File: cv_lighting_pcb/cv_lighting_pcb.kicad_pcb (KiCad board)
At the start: 2 copper layers, 27 parts, among them Q1 2N3906, U1 Current Driver, U2 Camera Input, U3 VO617A, U4 Barrel Jack

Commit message: added some notes to schematic
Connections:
- net Net-(U1-Vin+) renamed +30V
- R3 pad 1: Net-(U2-3) -> Net-(U2-PWM_Input)
- U2 pad 1: /PWM input -> Net-(U2-PWM_Input)
- U2 pad 2: GND -> Net-(U2-PWM_GND)
- U3 pad 2: Net-(U2-4) -> Net-(U2-PWM_GND)
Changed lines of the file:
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@@
   (net 11 "Net-(Q1-B)")
   (net 12 "Net-(Q1-C)")
-  (net 13 "/PWM input")
+  (net 13 "+30V")
   (net 14 "Net-(R3-Pad2)")
-  (net 15 "Net-(U1-Vin+)")
+  (net 15 "Net-(U2-PWM_Input)")
   (net 16 "GND")
-  (net 17 "Net-(U2-3)")
-  (net 18 "Net-(U2-4)")
-  (net 19 "unconnected-(U4-PadA2)")
-  (net 20 "unconnected-(U4-PadC)")
+  (net 17 "Net-(U2-PWM_GND)")
+  (net 18 "unconnected-(U4-PadA2)")
+  (net 19 "unconnected-(U4-PadC)")
   (footprint "cv_lighting_footprints:D3V3M1U2S9-7" (layer "F.Cu")
     (at 179.8828 130.7084)
@@
       (stroke (width 0.1) (type solid)) (layer "F.Fab"))
     (pad "1" smd roundrect (at -1.0375 0) (size 1.175 1.45) (layers "F.Cu" "F.Paste" "F.Mask") (roundrect_rratio 0.212766)
-      (net 15 "Net-(U1-Vin+)") (pintype "passive"))
+      (net 13 "+30V") (pintype "passive"))
     (pad "2" smd roundrect (at 1.0375 0) (size 1.175 1.45) (layers "F.Cu" "F.Paste" "F.Mask") (roundrect_rratio 0.212766)
       (net 16 "GND") (pintype "passive"))
@@
       (net 14 "Net-(R3-Pad2)") (pintype "passive"))
     (pad "2" smd rect (at -3.72 6.604) (size 2 1.78) (layers "F.Cu" "F.Paste" "F.Mask")
-      (net 18 "Net-(U2-4)") (pintype "passive"))
+      (net 17 "Net-(U2-PWM_GND)") (pintype "passive"))
     (pad "3" smd rect (at 3.9 6.604) (size 2 1.78) (layers "F.Cu" "F.Paste" "F.Mask")
       (net 9 "Net-(D15-A)") (pintype "passive"))
@@
       (net 10 "Net-(Q1-E)") (pinfunction "REF") (pintype "input") (solder_mask_margin 0.102))
     (pad "5" smd rect (at 6.6525 17.272 90) (size 1.02 1.905) (layers "F.Cu" "F.Paste" "F.Mask")
-      (net 15 "Net-(U1-Vin+)") (pinfunction "Vin+") (pintype "input") (solder_mask_margin 0.102))
+      (net 13 "+30V") (pinfunction "Vin+") (pintype "input") (solder_mask_margin 0.102))
     (pad "6" smd rect (at 9.9845 19.685 90) (size 1.02 1.905) (layers "F.Cu" "F.Paste" "F.Mask")
       (solder_mask_margin 0.102))
@@
       (stroke (width 0.1) (type solid)) (layer "F.Fab"))
     (pad "1" smd roundrect (at -1 0) (size 1.2 1.4) (layers "F.Cu" "F.Paste" "F.Mask") (roundrect_rratio 0.208333)
-      (net 17 "Net-(U2-3)") (pintype "passive"))
+      (net 15 "Net-(U2-PWM_Input)") (pintype "passive"))
     (pad "2" smd roundrect (at 1 0) (size 1.2 1.4) (layers "F.Cu" "F.Paste" "F.Mask") (roundrect_rratio 0.208333)
       (net 14 "Net-(R3-Pad2)") (pintype "passive"))
@@
     (pad "" np_thru_hole circle (at 0 2.25) (size 1.6 1.6) (drill 1.6) (layers "*.Cu" "*.Mask"))
     (pad "A1" smd rect (at -5.5 2.25) (size 2 2) (layers "F.Cu" "F.Paste" "F.Mask")
-      (net 15 "Net-(U1-Vin+)") (pintype "passive") (solder_mask_margin 0.102))
+      (net 13 "+30V") (pintype "passive") (solder_mask_margin 0.102))
     (pad "A2" smd rect (at -5.5 -3.95) (size 2 2) (layers "F.Cu" "F.Paste" "F.Mask")
-      (net 19 "unconnected-(U4-PadA2)") (pintype "passive") (solder_mask_margin 0.102))
+      (net 18 "unconnected-(U4-PadA2)") (pintype "passive") (solder_mask_margin 0.102))
     (pad "B" smd rect (at 5.5 2.25) (size 2 2) (layers "F.Cu" "F.Paste" "F.Mask")
       (net 16 "GND") (pintype "passive") (solder_mask_margin 0.102))
     (pad "C" smd rect (at 5.5 -3.95) (size 2 2) (layers "F.Cu" "F.Paste" "F.Mask")
-      (net 20 "unconnected-(U4-PadC)") (pintype "passive") (solder_mask_margin 0.102))
+      (net 19 "unconnected-(U4-PadC)") (pintype "passive") (solder_mask_margin 0.102))
   )
   (footprint "Connector_PinSocket_2.54mm:PinSocket_1x02_P2.54mm_Vertical_SMD_Pin1Left" (layer "F.Cu")
@@
       (stroke (width 0.1) (type solid)) (layer "F.Fab"))
     (pad "1" smd rect (at -1.65 -1.27) (size 1.9 1) (layers "F.Cu" "F.Paste" "F.Mask")
-      (net 13 "/PWM input") (pinfunction "Camera_input") (pintype "input"))
+      (net 15 "Net-(U2-PWM_Input)") (pinfunction "PWM_Input") (pintype "passive"))
     (pad "2" smd rect (at 1.65 1.27) (size 1.9 1) (layers "F.Cu" "F.Paste" "F.Mask")
-      (net 16 "GND") (pinfunction "GND") (pintype "input"))
+      (net 17 "Net-(U2-PWM_GND)") (pinfunction "PWM_GND") (pintype "passive"))
     (model "${KICAD6_3DMODEL_DIR}/Connector_PinSocket_2.54mm.3dshapes/PinSocket_1x02_P2.54mm_Vertical_SMD_Pin1Left.wrl"
       (offset (xyz 0 0 0))

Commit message: updates to lighting pcb
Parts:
- moved U2 39.9 mm to (121.0, 144.5)
- moved D11 32.0 mm to (242.4, 104.7)
- moved U1 31.2 mm to (118.7, 53.2)
- moved D4 30.9 mm to (237.5, 125.1)
- moved D3 28.0 mm to (238.8, 87.0)
- moved D12 26.4 mm to (227.8, 135.2)
- moved D5 26.0 mm to (212.7, 149.9)
- moved D10 24.1 mm to (227.2, 64.7)
- moved D2 23.5 mm to (213.4, 58.6)
- moved D13 21.9 mm to (190.7, 149.8)
- moved D9 21.1 mm to (195.4, 50.7)
- moved D14 18.4 mm to (161.5, 139.0)
- moved D6 18.1 mm to (174.0, 149.9)
- moved D7 13.8 mm to (148.0, 127.6)
- moved C2 13.7 mm to (131.4, 103.8)
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
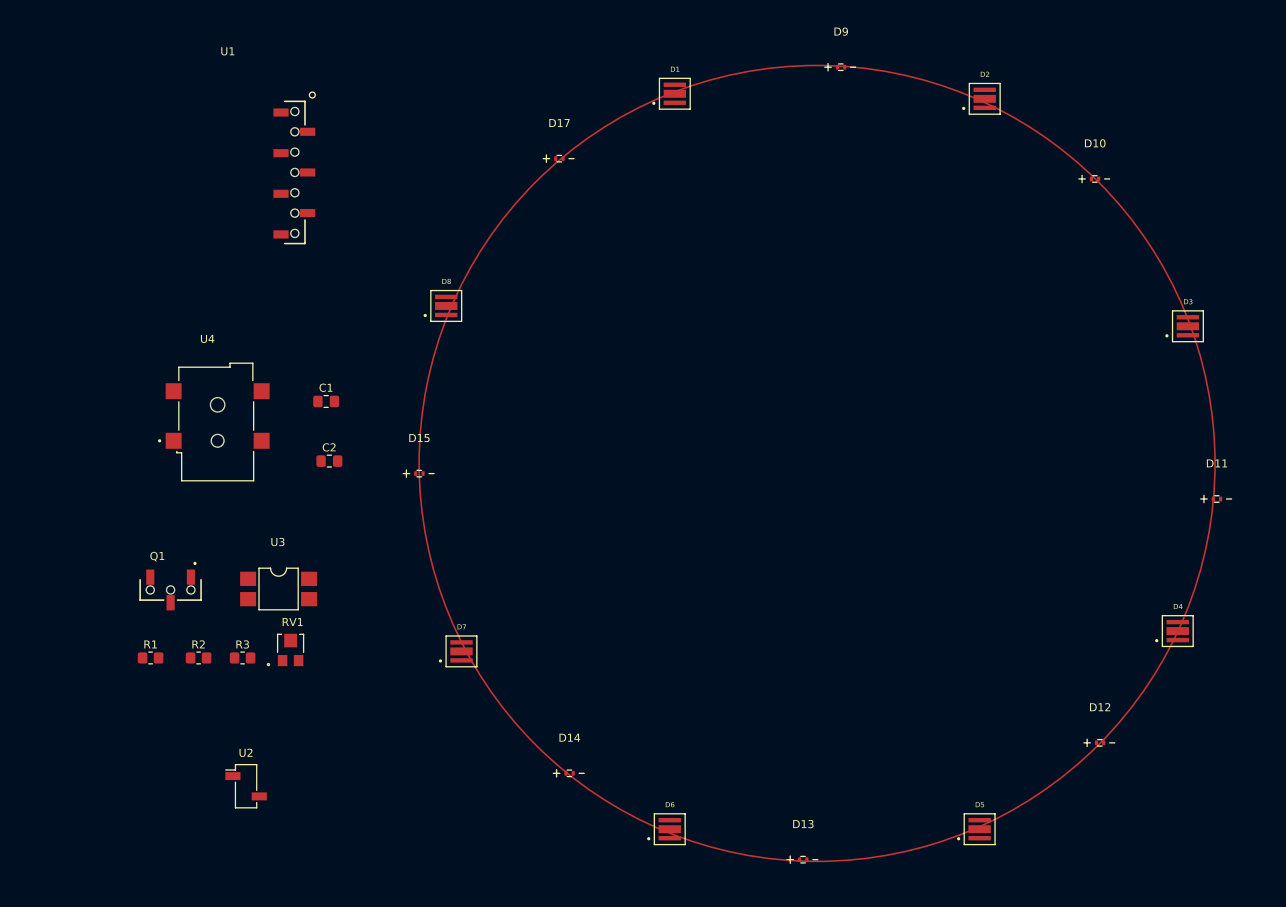
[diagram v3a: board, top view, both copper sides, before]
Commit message: initial routing and edge cuts for pcb
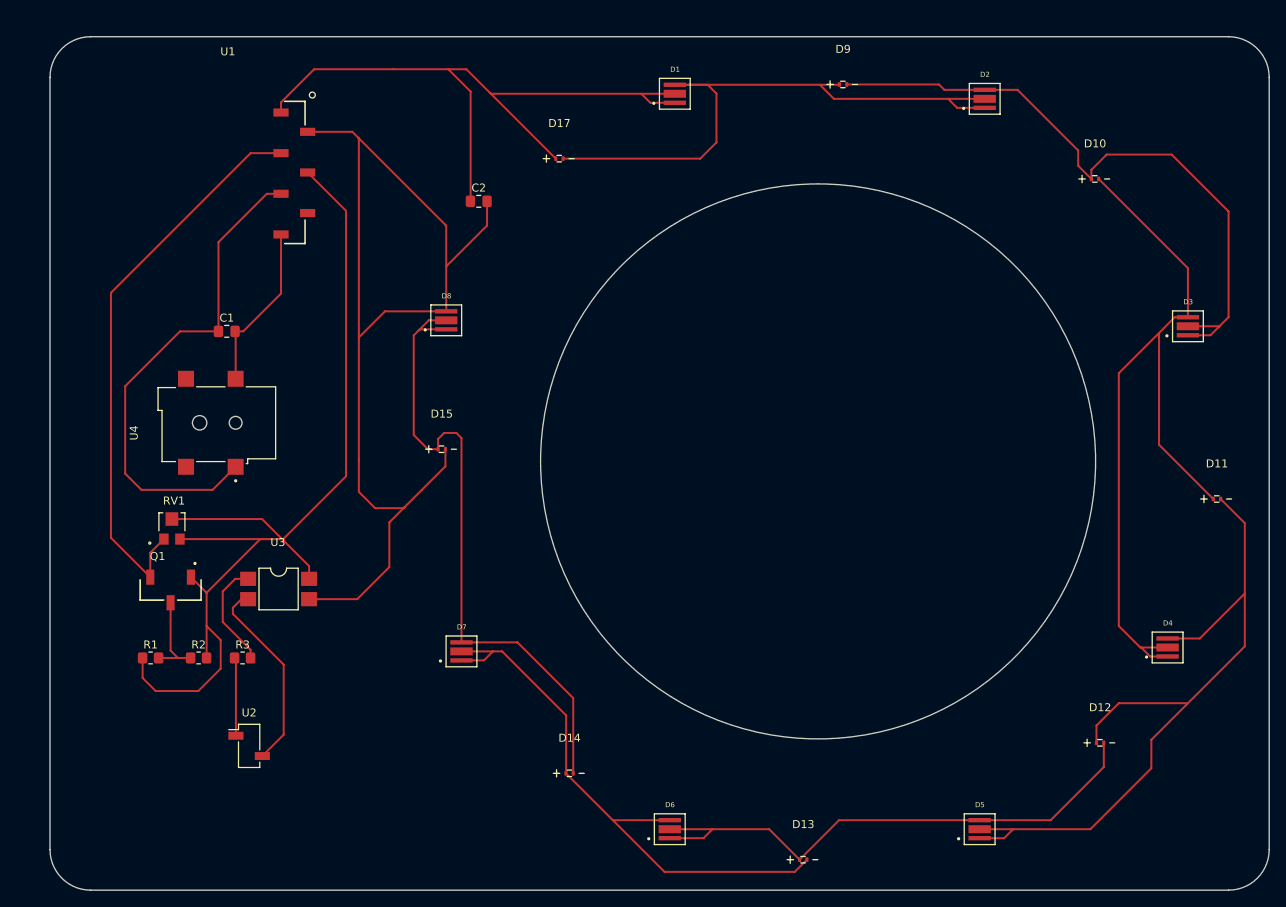
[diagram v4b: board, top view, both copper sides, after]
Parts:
- moved C2 37.5 mm to (150.1, 71.4)
- moved RV1 21.2 mm to (111.8, 112.3)
- moved C1 15.2 mm to (118.6, 87.6)
- moved U2 5.06 mm to (121.4, 139.4)
- moved D15 4.13 mm to (145.5, 98.5)
- moved D4 2.41 mm to (236.2, 127.1)
- moved D9 2.17 mm to (195.7, 52.9)
- moved D8 1.80 mm to (146.1, 86.3)
- turned U4 to 90 degrees
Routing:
- net Net-(D15-A): track 0.00 -> 135.6 mm
- net Net-(Q1-E): track 0.00 -> 128.4 mm
- net Net-(D10-A): track 0.00 -> 99.6 mm
- net Net-(D11-A): track 0.00 -> 95.8 mm
- net Net-(D1-A): track 0.00 -> 87.5 mm
- net Net-(D10-K): track 0.00 -> 81.8 mm
- net Net-(D14-A): track 0.00 -> 81.1 mm
- net Net-(D1-K): track 0.00 -> 78.7 mm
- net Net-(Q1-C): track 0.00 -> 71.5 mm
- net Net-(D13-A): track 0.00 -> 71.0 mm
- net Net-(D12-A): track 0.00 -> 69.5 mm
- net +30V: track 0.00 -> 62.7 mm
- net Net-(U2-PWM_GND): track 0.00 -> 24.6 mm
- net GND: track 0.00 -> 21.0 mm
- net Net-(R3-Pad2): track 0.00 -> 13.6 mm
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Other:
- board outline added: 152.4 x 106.7 mm
- board text added: "Double check radius of circle based on camera"
- board text added: "checker says every is connected but still double check also parts may change"

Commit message: updates to lighting pcb, now smaller
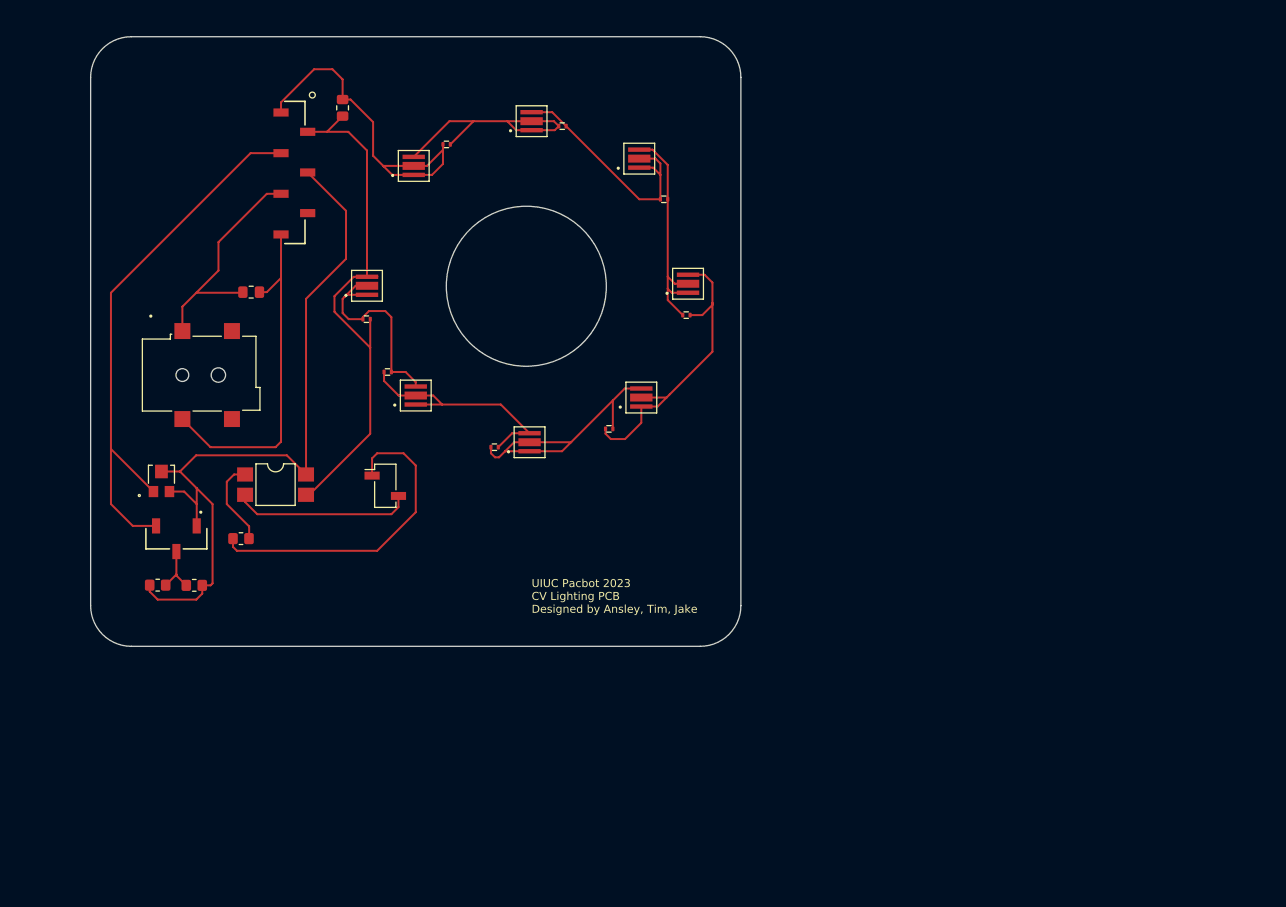
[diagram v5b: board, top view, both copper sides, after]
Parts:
- moved D4 75.2 mm to (176.3, 81.7)
- moved D12 72.8 mm to (166.4, 95.9)
- moved D3 71.7 mm to (170.2, 66.0)
- moved D11 70.2 mm to (176.1, 81.7)
- moved D5 68.6 mm to (170.4, 95.9)
- moved D13 64.4 mm to (152.1, 98.2)
- moved D2 56.7 mm to (156.7, 61.4)
- moved D14 55.1 mm to (138.7, 88.8)
- moved D10 53.9 mm to (173.3, 67.2)
- moved D6 51.4 mm to (156.5, 101.5)
- moved U2 36.7 mm to (138.4, 106.9)
- moved D9 35.5 mm to (160.6, 58.1)
- moved D1 33.9 mm to (142.0, 66.9)
- moved D7 32.5 mm to (142.2, 95.6)
- moved C2 20.6 mm to (133.1, 59.7), turned to -90 degrees
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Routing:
- net Net-(D10-A): track 99.6 -> 29.6 mm
- net Net-(D15-A): track 135.6 -> 67.1 mm
- net Net-(D11-A): track 95.8 -> 38.8 mm
- net Net-(D14-A): track 81.1 -> 26.7 mm
- net Net-(D10-K): track 81.8 -> 31.0 mm
- net Net-(D1-K): track 78.7 -> 31.5 mm
- net Net-(D1-A): track 87.5 -> 44.0 mm
- net Net-(D13-A): track 71.0 -> 29.9 mm
- net Net-(D12-A): track 69.5 -> 35.6 mm
- net +30V: track 62.7 -> 29.2 mm
- net Net-(Q1-E): track 128.4 -> 96.7 mm
- net Net-(U2-PWM_Input): track 10.2 -> 40.4 mm
- net GND: track 21.0 -> 43.4 mm
- net Net-(Q1-B): track 11.3 -> 6.63 mm
- net Net-(R3-Pad2): track 13.6 -> 10.9 mm
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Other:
- board size 152.4 x 106.7 mm -> 81.3 x 76.2 mm
- board text added: "UIUC Pacbot 2023 CV Lighting PCB Designed by Ansley, Tim, Jake"
- board text added: "checker says every is connected but still double check also parts may change 1in radius leds? camera rectangle with holes for mounting 20mm for camera 0.8in for led add holes for camera"
- board text removed: "checker says every is connected but still double check also parts may change"

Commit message: changes to lighting pcb
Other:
- board size 81.3 x 76.2 mm -> 81.3 x 73.7 mm
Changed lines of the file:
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@@
       (net 12 "Net-(Q1-C)") (pinfunction "C") (pintype "passive") (solder_mask_margin 0.102))
   )
+  (gr_arc (start 106.68 124.46) (mid 103.087898 122.972102) (end 101.6 119.38)
+    (stroke (width 0.1) (type default)) (layer "Edge.Cuts"))
   (gr_circle (center 167.5892 81.9912) (end 167.5892 81.9912)
     (stroke (width 0.1) (type default)) (fill none) (layer "Edge.Cuts"))
-  (gr_line (start 182.88 55.88) (end 182.88 121.92)
+  (gr_line (start 182.88 55.88) (end 182.88 119.38)
     (stroke (width 0.1) (type default)) (layer "Edge.Cuts"))
   (gr_line (start 106.68 50.8) (end 177.8 50.8)
@@
   (gr_arc (start 101.6 55.88) (mid 103.087898 52.287898) (end 106.68 50.8)
     (stroke (width 0.1) (type default)) (layer "Edge.Cuts"))
-  (gr_line (start 101.6 121.92) (end 101.6 55.88)
+  (gr_line (start 101.6 119.38) (end 101.6 55.88)
     (stroke (width 0.1) (type default)) (layer "Edge.Cuts"))
-  (gr_line (start 177.8 127) (end 106.68 127)
+  (gr_line (start 177.8 124.46) (end 106.68 124.46)
     (stroke (width 0.1) (type default)) (layer "Edge.Cuts"))
   (gr_circle (center 156.061042 81.9912) (end 166.061047 81.9912)
     (stroke (width 0.1) (type default)) (fill none) (layer "Edge.Cuts"))
-  (gr_arc (start 106.68 127) (mid 103.087898 125.512102) (end 101.6 121.92)
+  (gr_arc (start 182.88 119.38) (mid 181.392102 122.972102) (end 177.8 124.46)
     (stroke (width 0.1) (type default)) (layer "Edge.Cuts"))
   (gr_arc (start 177.8 50.8) (mid 181.392102 52.287898) (end 182.88 55.88)
     (stroke (width 0.1) (type default)) (layer "Edge.Cuts"))
-  (gr_arc (start 182.88 121.92) (mid 181.392102 125.512102) (end 177.8 127)
-    (stroke (width 0.1) (type default)) (layer "Edge.Cuts"))
   (gr_circle (center 156.061042 81.9912) (end 176.381042 81.9912)
     (stroke (width 0.1) (type default)) (fill none) (layer "F.Fab"))
-  (gr_text "UIUC Pacbot 2023\nCV Lighting PCB\nDesigned by Ansley, Tim, Jake" (at 156.718 122.936) (layer "F.SilkS")
+  (gr_text "UIUC Pacbot 2023\nCV Lighting PCB\nDesigned by Ansley, Tim, Jake" (at 154.94 121.92) (layer "F.SilkS")
     (effects (font (size 1 1) (thickness 0.15)) (justify left bottom))
   )

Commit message: changes to lighting pcb
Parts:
- moved D15 9.88 mm to (136.9, 92.0), turned to 180 degrees
- moved D13 2.31 mm to (149.9, 97.4)
- moved D11 1.56 mm to (175.7, 83.2)
- moved D9 1.30 mm to (161.8, 58.3)
- moved D12 1.00 mm to (165.6, 96.4)
- moved D5 0.97 mm to (170.2, 95.0)
- moved R3 0.80 mm to (119.6, 113.3), turned to 180 degrees
- moved D6 0.78 mm to (155.7, 101.3)
- moved D17 0.65 mm to (146.5, 59.8)
- moved D14 0.27 mm to (138.6, 88.5)
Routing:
- net Net-(D14-A): track 26.7 -> 15.4 mm
- net Net-(D1-A): track 44.0 -> 36.8 mm
- net Net-(D1-K): track 31.5 -> 24.6 mm
- net Net-(D10-A): track 29.6 -> 33.4 mm
- net Net-(D10-K): track 31.0 -> 27.2 mm
- net Net-(D15-A): track 67.1 -> 70.7 mm
- net Net-(U2-PWM_Input): track 40.4 -> 38.7 mm
- net Net-(D13-A): track 29.9 -> 28.2 mm
- net Net-(D12-A): track 35.6 -> 33.9 mm
- net Net-(D11-A): track 38.8 -> 40.5 mm
- net Net-(R3-Pad2): track 10.9 -> 9.53 mm
